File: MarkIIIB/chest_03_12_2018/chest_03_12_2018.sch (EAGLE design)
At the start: 11 parts, among them P100 503148-0890, U101 BNO055

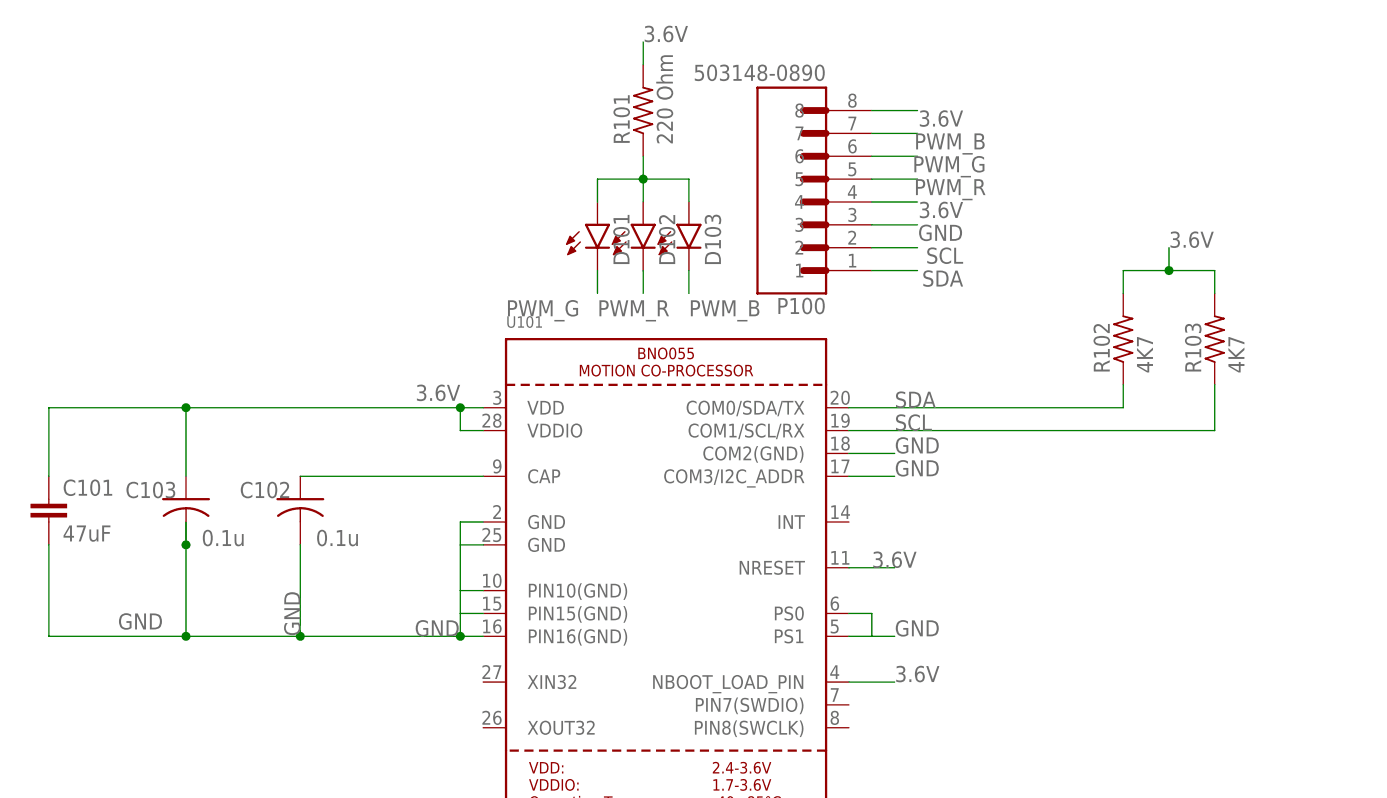
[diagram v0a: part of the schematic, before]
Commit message: Add Part Number ROllup Spreadsheets
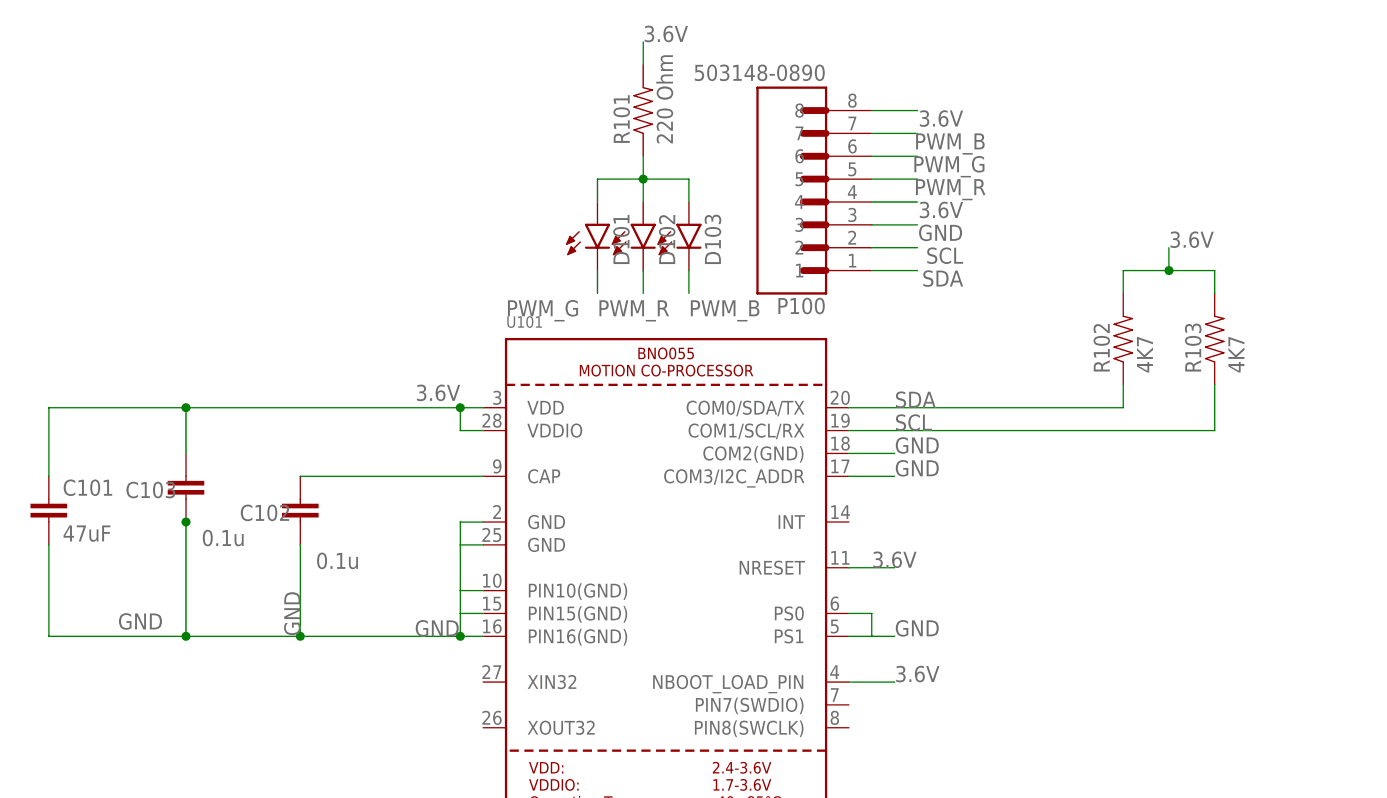
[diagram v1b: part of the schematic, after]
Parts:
- C102, C103: device rcl:C-USC0402 -> PatternAgents-ProtoPads:CAP0402-CAP
- R101, R102, R103: device rcl:R-US_R0402 -> PatternAgents-ProtoPads:RESISTOR0402-TYP
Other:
- moved on the sheet: C103
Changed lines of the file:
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@@
 </classes>
 <parts>
-<part name="R101" library="rcl" deviceset="R-US_" device="R0402" value="220 Ohm"/>
+<part name="R101" library="PatternAgents-ProtoPads" deviceset="RESISTOR" device="0402-TYP" value="220 Ohm"/>
 <part name="P100" library="503148-0890" deviceset="503148-0890" device=""/>
 <part name="U101" library="microbuilder" deviceset="BNO055" device="" value="BNO055"/>
-<part name="C103" library="rcl" deviceset="C-US" device="C0402" value="0.1u"/>
-<part name="C102" library="rcl" deviceset="C-US" device="C0402" value="0.1u"/>
+<part name="C103" library="PatternAgents-ProtoPads" deviceset="CAP" device="0402-CAP" value="0.1u"/>
+<part name="C102" library="PatternAgents-ProtoPads" deviceset="CAP" device="0402-CAP" value="0.1u"/>
 <part name="FRAME1" library="PatternAgents-Beautify" deviceset="FRAME_ASIZE_LANDSCAPE" device=""/>
 <part name="D101" library="SparkFun-LED" deviceset="LED" device="0603"/>
@@
 <part name="D103" library="SparkFun-LED" deviceset="LED" device="0603"/>
 <part name="C101" library="PatternAgents-ProtoPads" deviceset="CAP" device="1206" value="47uF"/>
-<part name="R102" library="rcl" deviceset="R-US_" device="R0402" value="4K7"/>
-<part name="R103" library="rcl" deviceset="R-US_" device="R0402" value="4K7"/>
+<part name="R102" library="PatternAgents-ProtoPads" deviceset="RESISTOR" device="0402-TYP" value="4K7"/>
+<part name="R103" library="PatternAgents-ProtoPads" deviceset="RESISTOR" device="0402-TYP" value="4K7"/>
 </parts>
 <sheets>
@@
 </plain>
 <instances>
-<instance part="R101" gate="G$1" x="127" y="147.32" rot="R90"/>
+<instance part="R101" gate="R" x="127" y="147.32" rot="R90"/>
 <instance part="P100" gate="G$1" x="147.32" y="137.16" rot="R180"/>
 <instance part="U101" gate="G$1" x="129.54" y="96.52"/>
@@
 <attribute name="VALUE" x="82.804" y="100.711" size="1.778" layer="96" rot="R180"/>
 </instance>
-<instance part="C102" gate="G$1" x="88.9" y="104.14" smashed="yes">
-<attribute name="NAME" x="87.884" y="106.045" size="1.778" layer="95" rot="R180"/>
-<attribute name="VALUE" x="95.504" y="100.711" size="1.778" layer="96" rot="R180"/>
+<instance part="C102" gate="G$1" x="88.9" y="101.6" smashed="yes">
+<attribute name="NAME" x="87.884" y="103.505" size="1.778" layer="95" rot="R180"/>
+<attribute name="VALUE" x="95.504" y="98.171" size="1.778" layer="96" rot="R180"/>
 </instance>
 <instance part="FRAME1" gate="G$2" x="172.72" y="0"/>
@@
 <attribute name="VALUE" x="62.484" y="99.441" size="1.778" layer="96"/>
 </instance>
-<instance part="R102" gate="G$1" x="180.34" y="121.92" rot="R90"/>
-<instance part="R103" gate="G$1" x="190.5" y="121.92" rot="R90"/>
+<instance part="R102" gate="R" x="180.34" y="121.92" rot="R90"/>
+<instance part="R103" gate="R" x="190.5" y="121.92" rot="R90"/>
 </instances>
 <busses>
@@
 <segment>
 <pinref part="C103" gate="G$1" pin="2"/>
-<wire x1="76.2" y1="99.06" x2="76.2" y2="101.6" width="0.1524" layer="91"/>
 <label x="73.66" y="91.44" size="1.778" layer="95" rot="R180"/>
 <pinref part="U101" gate="G$1" pin="GND@1"/>
@@
 <junction x="106.68" y="88.9"/>
 <junction x="88.9" y="88.9"/>
-<wire x1="76.2" y1="99.06" x2="76.2" y2="88.9" width="0.1524" layer="91"/>
-<junction x="76.2" y="99.06"/>
+<wire x1="76.2" y1="101.6" x2="76.2" y2="88.9" width="0.1524" layer="91"/>
+<junction x="76.2" y="101.6"/>
 <junction x="76.2" y="88.9"/>
 </segment>
@@
 <pinref part="C103" gate="G$1" pin="1"/>
 <label x="106.68" y="116.84" size="1.778" layer="95" rot="R180"/>
-<wire x1="76.2" y1="106.68" x2="76.2" y2="114.3" width="0.1524" layer="91"/>
+<wire x1="76.2" y1="109.22" x2="76.2" y2="114.3" width="0.1524" layer="91"/>
 <wire x1="76.2" y1="114.3" x2="106.68" y2="114.3" width="0.1524" layer="91"/>
 <junction x="106.68" y="114.3"/>
@@
 </segment>
 <segment>
-<pinref part="R101" gate="G$1" pin="2"/>
+<pinref part="R101" gate="R" pin="2"/>
 <wire x1="127" y1="152.4" x2="127" y2="154.94" width="0.1524" layer="91"/>
 <label x="127" y="154.94" size="1.778" layer="95"/>
 </segment>
 <segment>
-<pinref part="R102" gate="G$1" pin="2"/>
+<pinref part="R102" gate="R" pin="2"/>
 <wire x1="180.34" y1="127" x2="180.34" y2="129.54" width="0.1524" layer="91"/>
-<pinref part="R103" gate="G$1" pin="2"/>
+<pinref part="R103" gate="R" pin="2"/>
 <wire x1="180.34" y1="129.54" x2="185.42" y2="129.54" width="0.1524" layer="91"/>
 <wire x1="185.42" y1="129.54" x2="190.5" y2="129.54" width="0.1524" layer="91"/>
@@
 <pinref part="U101" gate="G$1" pin="COM0/SDA/TX"/>
 <label x="154.94" y="114.3" size="1.778" layer="95"/>
-<pinref part="R102" gate="G$1" pin="1"/>
+<pinref part="R102" gate="R" pin="1"/>
 <wire x1="149.86" y1="114.3" x2="180.34" y2="114.3" width="0.1524" layer="91"/>
 <wire x1="180.34" y1="114.3" x2="180.34" y2="116.84" width="0.1524" layer="91"/>
@@
 <pinref part="U101" gate="G$1" pin="COM1/SCL/RX"/>
 <label x="154.94" y="111.76" size="1.778" layer="95"/>
-<pinref part="R103" gate="G$1" pin="1"/>
+<pinref part="R103" gate="R" pin="1"/>
 <wire x1="149.86" y1="111.76" x2="190.5" y2="111.76" width="0.1524" layer="91"/>
 <wire x1="190.5" y1="111.76" x2="190.5" y2="116.84" width="0.1524" layer="91"/>
@@
 <net name="N$1" class="0">
 <segment>
-<pinref part="R101" gate="G$1" pin="1"/>
+<pinref part="R101" gate="R" pin="1"/>
 <pinref part="D102" gate="G$1" pin="A"/>
 <wire x1="127" y1="142.24" x2="127" y2="139.7" width="0.1524" layer="91"/>
